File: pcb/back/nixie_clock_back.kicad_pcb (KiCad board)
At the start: 2 copper layers, 110 x 50 mm, 22 parts, among them J1 Conn_01x10_Male, J2 Conn_01x10_Male, J3 ICSP, J4 5V_IN, SW1 BTN2, SW2 BTN1, U1 ATmega328P-PU, U2 DS1307, Y1 32768Hz

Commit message: Final PCB tweaks
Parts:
- moved BT1 2.31 mm to (104.6, 62.8)
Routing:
- net Net-(BT1-Pad1): track 18.2 -> 0.00 mm
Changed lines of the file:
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@@
     (thickness 1.6)
     (drawings 7)
-    (tracks 153)
+    (tracks 151)
     (zones 0)
     (modules 22)
@@
   )
   (module Battery:BatteryHolder_Keystone_103_1x20mm (layer B.Cu)
-    (at 102.28 62.87 180)
+    (at 104.59 62.79 180)
     (descr http://www.keyelco.com/product-pdf.cfm?p=719)
     (tags "Keystone type 103 battery holder")
@@
       (effects (font (size 1 1) (thickness 0.15)))
     )
-    (fp_text value 5V_IN (at 2.25 5) (layer F.SilkS)
+    (fp_text value 5V_IN (at 2.25 5) (layer F.SilkS) hide
       (effects (font (size 1 1) (thickness 0.15)))
     )
@@
     )
   )
-  (gr_text ⏚ (at 112.53 54.84) (layer F.SilkS)
+  (gr_text ⏚ (at 112.46 51.8) (layer F.SilkS)
     (effects (font (size 1 1) (thickness 0.2)) (justify mirror))
   )
-  (gr_text +5V (at 98.87 54.58) (layer F.SilkS)
+  (gr_text +5V (at 98.92 51.86) (layer F.SilkS)
     (effects (font (size 1 1) (thickness 0.2)) (justify mirror))
   )
@@
   (gr_line (start 160 50) (end 160 100) (layer Edge.Cuts) (width 0.05))
   (gr_line (start 50 50) (end 160 50) (layer Edge.Cuts) (width 0.05))
-  (segment (start 102.28 70.2) (end 110 77.92) (width 0.25) (layer B.Cu) (net 2))
-  (segment (start 102.28 62.87) (end 102.28 70.2) (width 0.25) (layer B.Cu) (net 2))
   (segment (start 72.4 71) (end 72.37 71.03) (width 0.5) (layer F.Cu) (net 3))
   (segment (start 75 71) (end 72.4 71) (width 0.5) (layer F.Cu) (net 3))

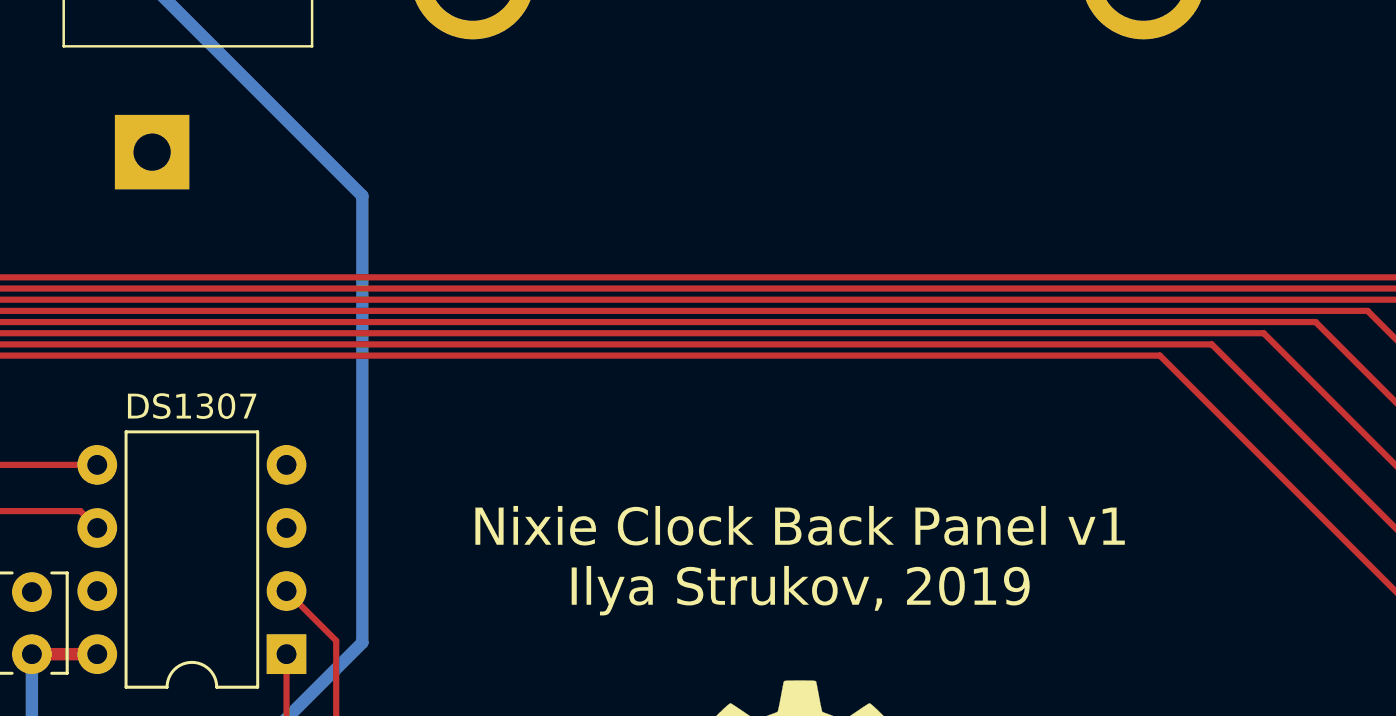
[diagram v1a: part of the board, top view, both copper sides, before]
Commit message: Add missing PCB trace
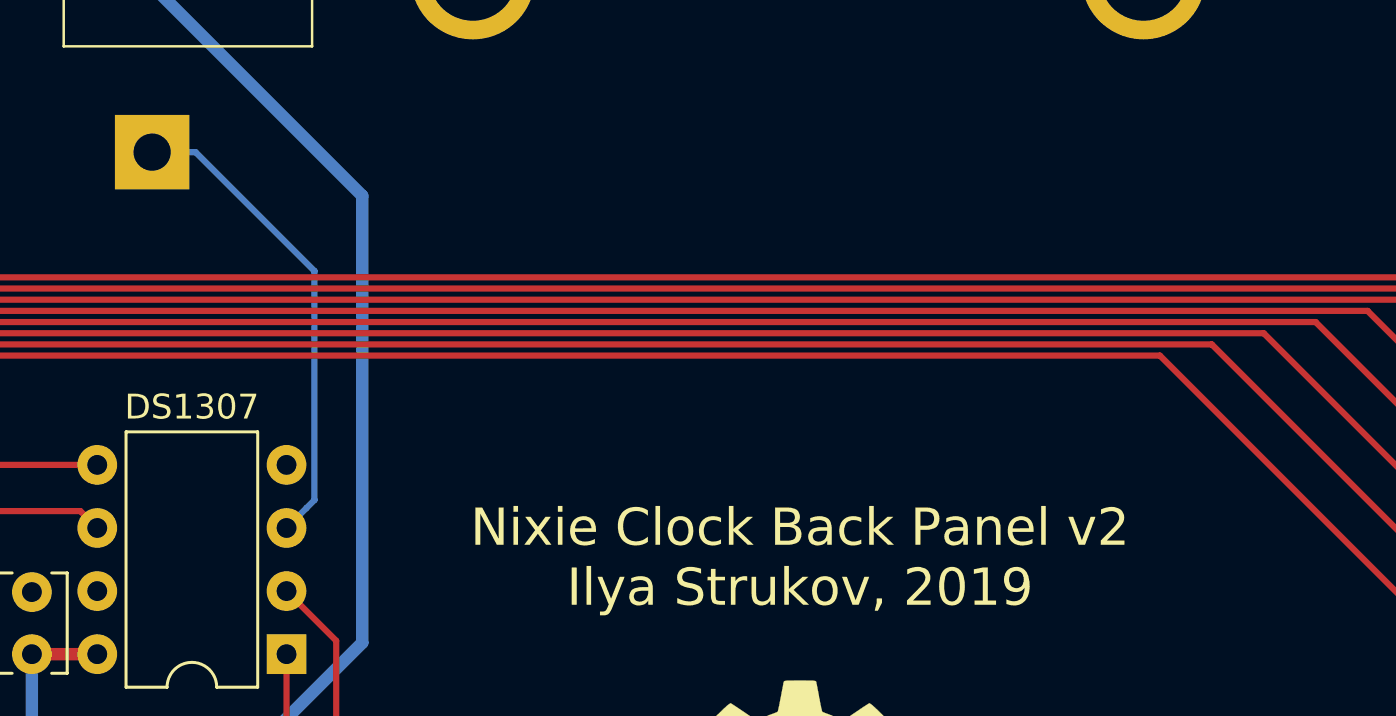
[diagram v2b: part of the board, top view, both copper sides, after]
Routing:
- net Net-(BT1-Pad1): track 0.00 -> 19.3 mm
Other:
- board text added: "Nixie Clock Back Panel v2 Ilya Strukov, 2019"
- board text removed: "Nixie Clock Back Panel v1 Ilya Strukov, 2019"
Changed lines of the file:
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@@
     (thickness 1.6)
     (drawings 7)
-    (tracks 151)
+    (tracks 156)
     (zones 0)
     (modules 22)
@@
     (effects (font (size 1 1) (thickness 0.2)) (justify mirror))
   )
-  (gr_text "Nixie Clock Back Panel v1\nIlya Strukov, 2019" (at 130.67 79.11) (layer F.SilkS)
+  (gr_text "Nixie Clock Back Panel v2\nIlya Strukov, 2019" (at 130.67 79.11) (layer F.SilkS)
     (effects (font (size 1.5 1.5) (thickness 0.3)))
   )
@@
   (gr_line (start 160 50) (end 160 100) (layer Edge.Cuts) (width 0.05))
   (gr_line (start 50 50) (end 160 50) (layer Edge.Cuts) (width 0.05))
+  (segment (start 110.799999 77.120001) (end 110 77.92) (width 0.25) (layer B.Cu) (net 2))
+  (segment (start 111.125001 67.575001) (end 111.125001 76.794999) (width 0.25) (layer B.Cu) (net 2))
+  (segment (start 106.34 62.79) (end 111.125001 67.575001) (width 0.25) (layer B.Cu) (net 2))
+  (segment (start 111.125001 76.794999) (end 110.799999 77.120001) (width 0.25) (layer B.Cu) (net 2))
+  (segment (start 104.59 62.79) (end 106.34 62.79) (width 0.25) (layer B.Cu) (net 2))
   (segment (start 72.4 71) (end 72.37 71.03) (width 0.5) (layer F.Cu) (net 3))
   (segment (start 75 71) (end 72.4 71) (width 0.5) (layer F.Cu) (net 3))

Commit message: Fix minor issues on the back PCB
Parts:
- moved R1 6.02 mm to (84.4, 83.3)
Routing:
- net VCC: track 165.7 -> 189.8 mm
- net /BTN2: track 68.6 -> 48.8 mm
- net /SCL: track 42.7 -> 56.5 mm
- net /SDA: track 42.6 -> 51.4 mm
- net GND: track 0.00 -> 5.50 mm
- net /BTN1: track 40.4 -> 37.3 mm
- net /RESET: track 61.2 -> 59.4 mm
- net /MISO: track 16.7 -> 15.4 mm
- net /TUBE4C: track 105.2 -> 104.2 mm
- net /SCK: track 18.8 -> 18.1 mm
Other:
- board text added: "Nixie Clock Back Panel v2 Ilya Strukov, 2020"
- board text removed: "Nixie Clock Back Panel v2 Ilya Strukov, 2019"

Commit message: back pcb: upgrade to kicad 6, add measurements
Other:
- net class Default removed
- net class HighVoltage removed
- net class Power removed
